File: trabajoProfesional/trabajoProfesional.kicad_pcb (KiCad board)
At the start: 2 copper layers, 66.2 x 25.4 mm, 47 parts, among them M0 1501

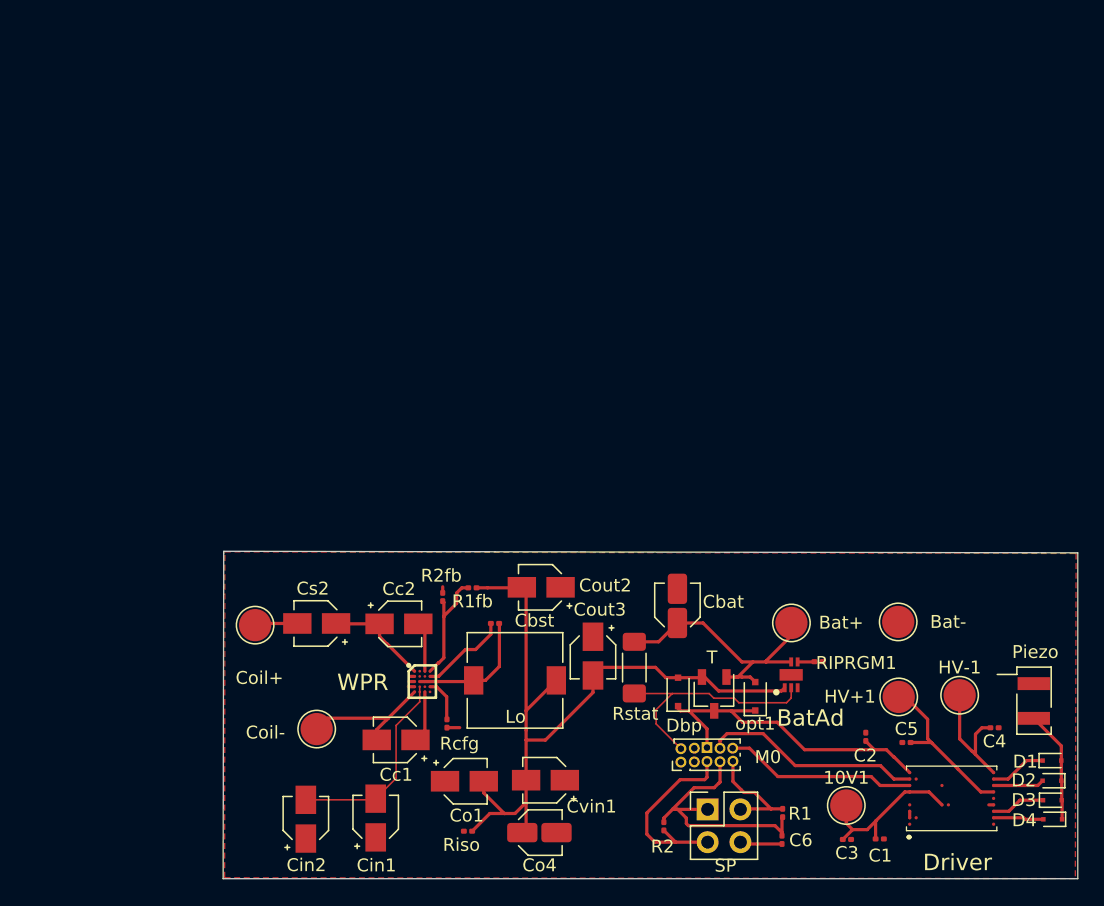
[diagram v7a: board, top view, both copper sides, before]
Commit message: achicamiento de placa a un cuarto del tamanio anterior
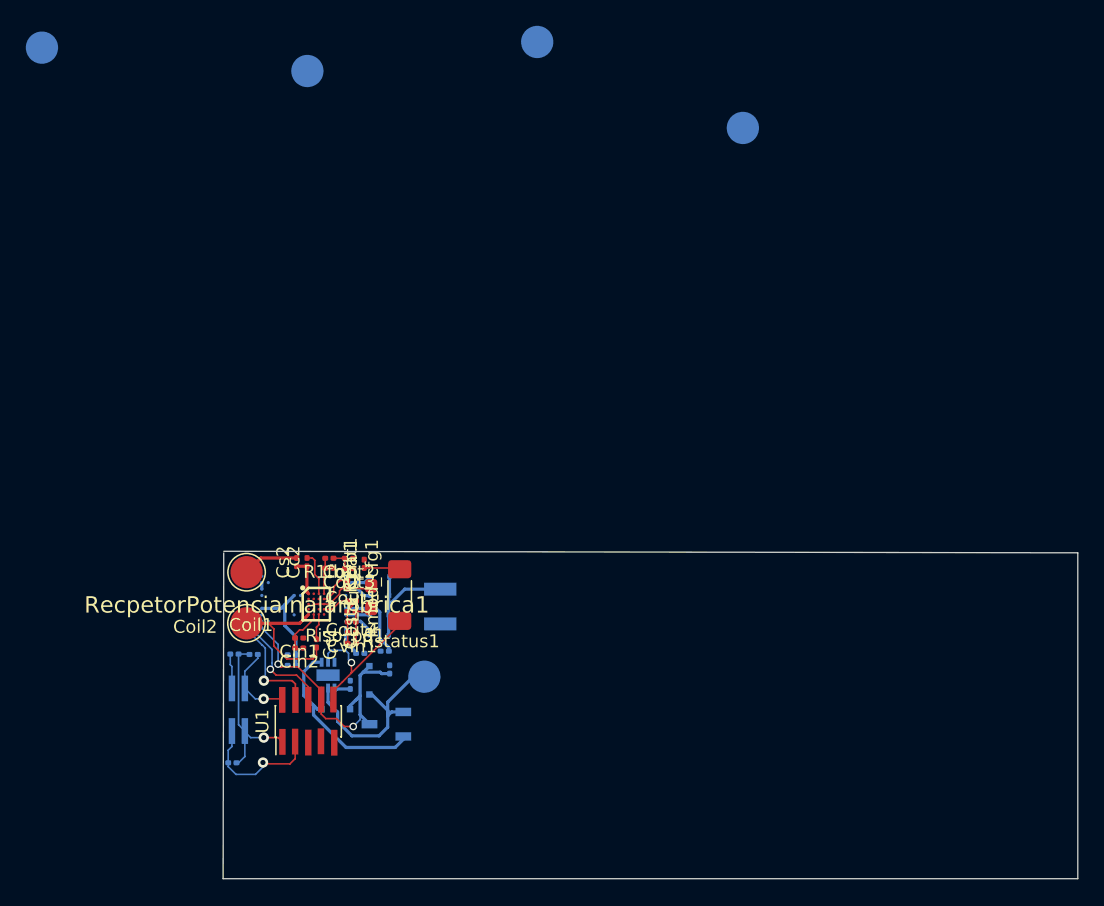
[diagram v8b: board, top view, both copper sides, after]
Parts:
- removed BatAd: SC810ULTRT, SC810:SON50P200X200X60-7N-D
- removed Cbat: 2.2u, Capacitor_SMD:C_Elec_3x5.4
- removed Cbst: 47n, Capacitor_SMD:C_0201_0603Metric
- removed Co1, Co4: 22u, Capacitor_SMD:CP_Elec_3x5.3
- removed Coil+, Coil-: Conn_01x01_Male, TestPoint:TestPoint_Pad_D2.5mm
- removed Dbp: D_Schottky, Diode_SMD:D_SOD-323F
- removed Driver: HV7360GA-G, HV7360:HV7360GAG
- removed Lo: 4.7u, Inductor_SMD:L_7.3x7.3_H3.5
- removed M0: 1501, Connector_PinHeader_1.00mm:PinHeader_2x05_P1.00mm_Vertical
- removed R1fb: 46k, Resistor_SMD:R_0201_0603Metric
- removed R2fb: 10k, Resistor_SMD:R_0201_0603Metric
- removed Rcfg: 60k, Resistor_SMD:R_0201_0603Metric
- removed Riso: R, Resistor_SMD:R_0201_0603Metric
- removed Rstat: R, Resistor_SMD:R_1806_4516Metric
- removed SP: MS583730BA01-50, Connector_PinHeader_2.54mm:PinHeader_2x02_P2.54mm_Vertical
- removed T: MPMOS, Package_TO_SOT_SMD:TSOT-23
- removed WPR: TS51223-M000WCSR, TS51223:BGA20C40P4X5_190X230X58
- added AdministracionBateria1: SC810ULTRT, SC810:SON50P200X200X60-7N-D, B.Cu at (66.5, 68.7)
- added Cbat1: 2.2u, Capacitor_SMD:C_0201_0603Metric, F.Cu at (69.3, 60.1)
- added Cbst1: 47n, Capacitor_SMD:C_0201_0603Metric, F.Cu at (68.0, 61.7)
- added Coil1: Conn_01x01_Male, TestPoint:TestPoint_Pad_D2.5mm, F.Cu at (60.2, 60.7)
- added Coil2: Conn_01x01_Male, TestPoint:TestPoint_Pad_D2.5mm, F.Cu at (60.2, 64.7)
- added Cout1: 22u, Capacitor_SMD:C_0201_0603Metric, F.Cu at (68.3, 63.8)
- added Cout4: 22u, Capacitor_SMD:C_0201_0603Metric, F.Cu at (68.3, 66.2)
- added DbyPass1: D_Schottky, Diode_SMD:D_SOD-323F, B.Cu at (67.1, 71.3)
- added DriverPotencia1: HV7360GA-G, HV7360:HV7360GAG, B.Cu at (64.6, 63.0)
- added Lout1: 4.7u, Inductor_SMD:L_0603_1608Metric_Pad1.05x0.95mm_HandSolder, F.Cu at (69.8, 62.6)
- added R1fb1: 46k, Resistor_SMD:R_0201_0603Metric, F.Cu at (66.6, 59.6)
- added R2fb1: 10k, Resistor_SMD:R_0201_0603Metric, F.Cu at (66.6, 60.4)
- added RecpetorPotenciaInalambrica1: TS51223-M000WCSR, TS51223:BGA20C40P4X5_190X230X58, F.Cu at (65.6, 63.2)
- added Riso_pd1: R, Resistor_SMD:R_0201_0603Metric, F.Cu at (68.3, 64.6)
- added Rmod_cfg1: 60k, Resistor_SMD:R_0201_0603Metric, F.Cu at (68.3, 63.0)
- added Rstatus1: R, Resistor_SMD:R_1806_4516Metric, F.Cu at (72.0, 62.5)
- added SensorPresion1: MS583730BA01-50, Connector_PinHeader_1.00mm:PinHeader_2x02_P1.00mm_Vertical_SMD, B.Cu at (59.5, 71.4)
- added T1: MPMOS, Package_TO_SOT_SMD:TSOT-23, B.Cu at (71.0, 72.5)
- added U1: 1501, Connector_PinHeader_1.00mm:PinHeader_2x05_P1.00mm_Vertical_SMD, F.Cu at (65.0, 72.3)
- 10V1, C1, C2, C3, C4, C5, C6, D1, D2, D3, D4, HV+1, HV-1, R1, R2, RIPRGM1, opt1: moved to B.Cu
- BatPositivo1: renamed from Bat+; moved to B.Cu
- Cc1, Cc2, Cin1, Cin2, Cout2, Cout3, Cs2: footprint Capacitor_SMD:CP_Elec_3x5.3 -> Capacitor_SMD:C_0201_0603Metric
- Cvin1: footprint Capacitor_SMD:C_Elec_3x5.4 -> Capacitor_SMD:C_0201_0603Metric
- PiezoElectrico1: renamed from Piezo; moved to B.Cu
- batGND1: renamed from Bat-; moved to B.Cu
- moved 10V1 85.6 mm to (44.3, 20.1)
- moved HV+1 66.7 mm to (64.9, 21.9)
- moved HV-1 60.3 mm to (82.7, 19.6)
- moved D4 55.4 mm to (70.5, 61.0)
- moved D3 54.5 mm to (70.5, 62.5)
- moved D2 53.7 mm to (70.5, 64.0)
- moved D1 53.0 mm to (70.5, 65.6)
- moved C4 49.5 mm to (69.0, 67.0)
- moved C1 47.7 mm to (63.7, 67.1), turned to 180 degrees
- moved PiezoElectrico1 46.5 mm to (75.2, 63.4)
- moved C3 45.1 mm to (63.7, 67.9), turned to 0 degrees
- moved C6 44.8 mm to (59.2, 67.1), turned to 0 degrees
- moved R1 42.8 mm to (60.7, 67.1), turned to 0 degrees
- moved C5 41.0 mm to (70.9, 66.8)
- moved batGND1 40.1 mm to (98.6, 26.3)
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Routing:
- net Net-(AdministracionBateria1-Pad1): track 58.4 -> 20.1 mm
- net Net-(Cin1-Pad2): track 15.5 -> 3.35 mm
- net /Salida/SP1ONOFF: track 17.0 -> 8.95 mm, vias 0 -> 1
- net Net-(C6-Pad2): track 20.9 -> 13.1 mm, vias 0 -> 1
- net -HV: track 10.0 -> 2.31 mm
- net +HV: track 13.0 -> 6.07 mm
- net /Bateria/Cargando: track 19.0 -> 12.3 mm, vias 0 -> 1
- net Net-(R1fb1-Pad2): track 9.23 -> 2.79 mm
- net Net-(Cc2-Pad1): track 8.19 -> 2.99 mm
- net 10V: track 13.1 -> 7.96 mm
- net /Salida/SN1ONOFF: track 14.9 -> 9.96 mm, vias 0 -> 1
- net Net-(Cbst1-Pad1): track 9.99 -> 5.18 mm
- net SCLPresion: track 14.9 -> 10.4 mm, vias 0 -> 1
- net Net-(Cbst1-Pad2): track 6.90 -> 2.68 mm
- net /Salida/Alimentacion: track 26.4 -> 22.9 mm, vias 0 -> 2
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- removed copper zone on F.Cu, net GND
